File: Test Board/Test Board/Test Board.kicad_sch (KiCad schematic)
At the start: 51 parts, among them J10 Conn_Coaxial_Power, J11 Conn_Coaxial_Power, J13 Conn_Coaxial_Power, J8 Screw_Terminal_01x03, J9 Conn_Coaxial_Power, SW10 SW_SPDT, SW7 SW_SPDT, SW8 SW_SPDT, SW9 SW_SPDT, U27 OPA189, U28 BUF634A, U29 OPA189, U30 OPA189, U34 INA849

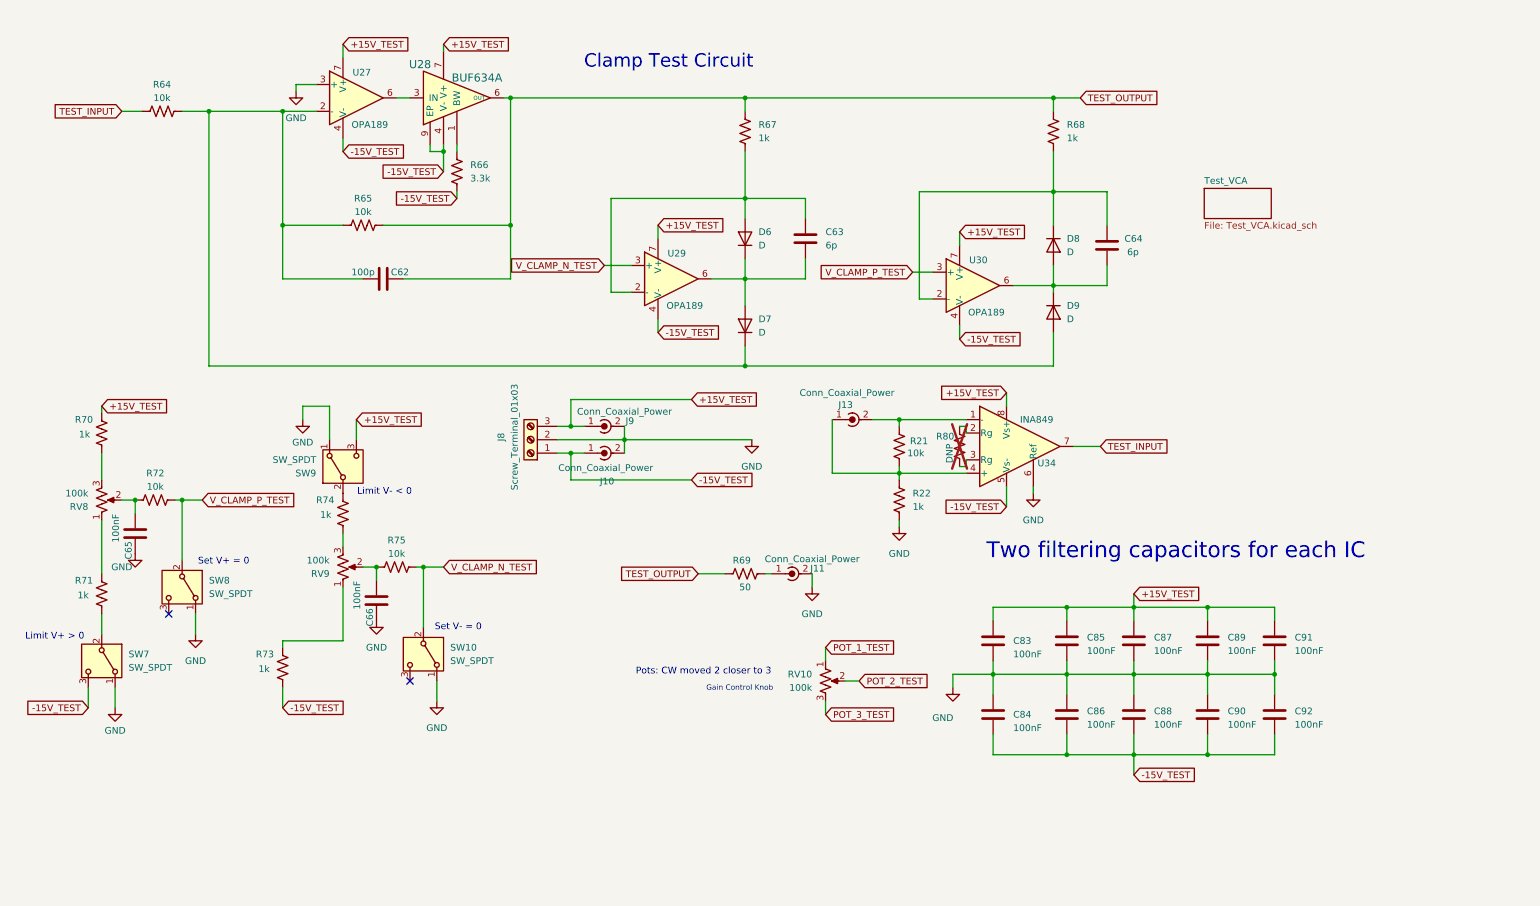
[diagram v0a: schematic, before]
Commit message: Removed LH circuit, added anti-windup test circuit, simplified voltage control mechanism
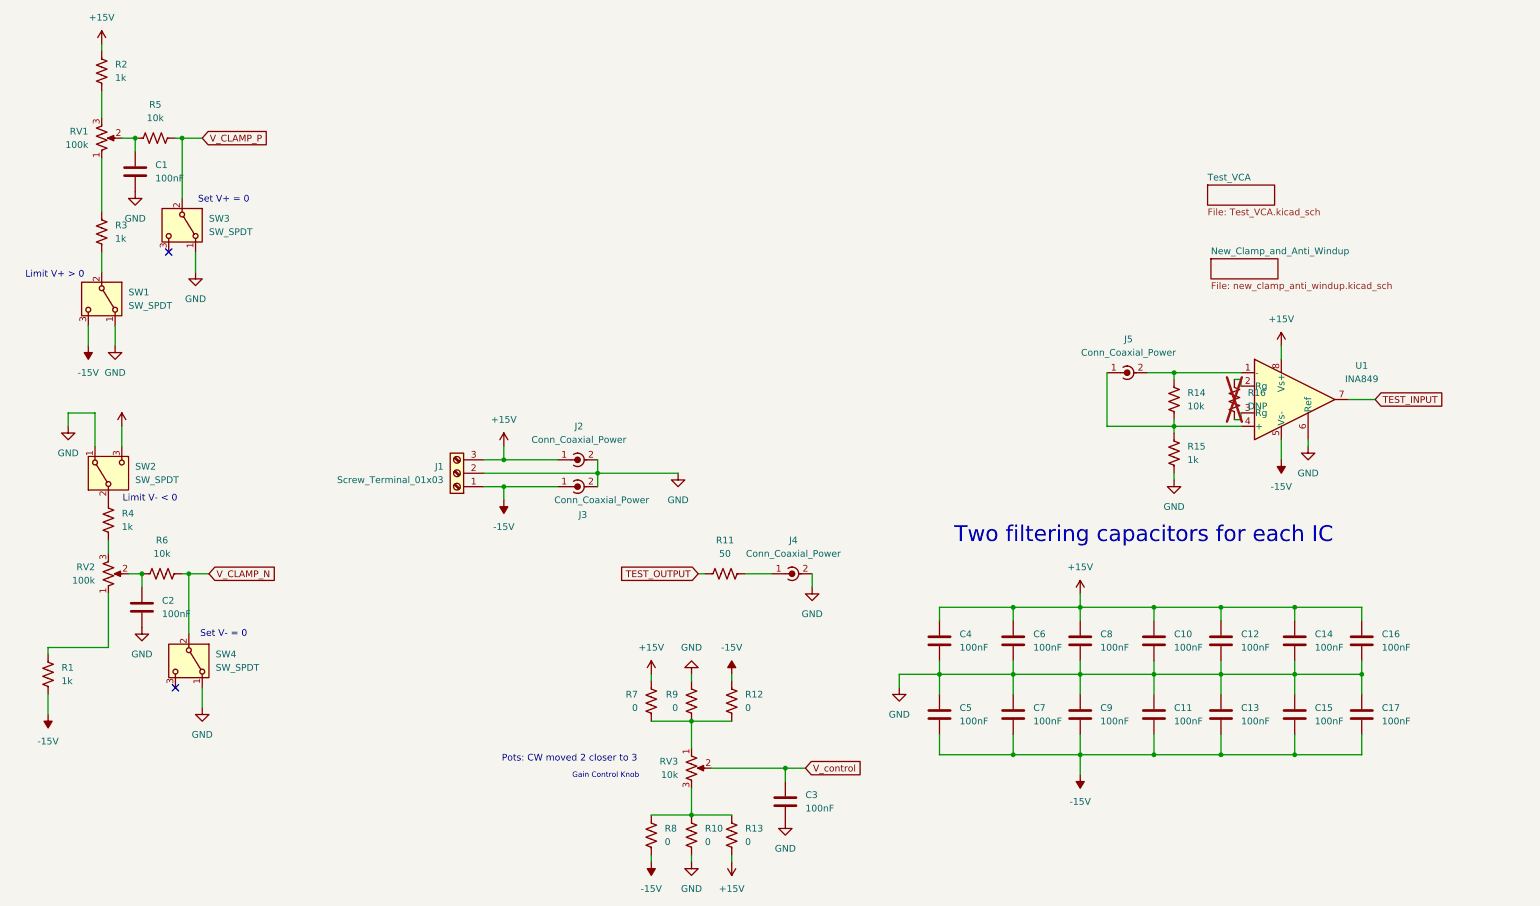
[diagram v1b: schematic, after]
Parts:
- removed C62: 100p, Capacitor_SMD:C_0805_2012Metric, symbol Device:C
- removed C63, C64: 6p, Capacitor_SMD:C_0805_2012Metric, symbol Device:C
- removed D6, D7, D8, D9: D, Package_TO_SOT_SMD:TSOT-23, symbol Device:D
- removed R64, R65: 10k, Resistor_SMD:R_0805_2012Metric, symbol Device:R_US
- removed R66: 3.3k, Resistor_SMD:R_0805_2012Metric, symbol Device:R_US
- removed R67, R68: 1k, Resistor_SMD:R_0805_2012Metric, symbol Device:R_US
- removed U27, U29, U30: OPA189, Package_SO:SOIC-8_3.9x4.9mm_P1.27mm, symbol Amplifier_Operational:OPA330xxD
- removed U28: BUF634A, Custom_Footprints:BUF634AIDDAR, symbol local_lib:BUF634A
- added C14, C15, C16, C17, C3: 100nF, Capacitor_SMD:C_0805_2012Metric, symbol Device:C
- added R10, R12, R13, R7, R8, R9: 0, Resistor_SMD:R_0805_2012Metric, symbol Device:R_US
- RV3: renamed from RV10; value 100k -> 10k
- renumbered C65 to C1, C89 to C10, C90 to C11, C91 to C12, C92 to C13, C66 to C2, C83 to C4, C84 to C5, C85 to C6, C86 to C7, C87 to C8, C88 to C9, J8 to J1, J9 to J2, J10 to J3, J11 to J4, J13 to J5, R73 to R1, R69 to R11, R21 to R14, R22 to R15, R80 to R16, R70 to R2, R71 to R3, R74 to R4, R72 to R5, R75 to R6, RV8 to RV1, RV9 to RV2, SW7 to SW1, SW9 to SW2, SW8 to SW3, SW10 to SW4, U34 to U1
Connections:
- net GND: now also C14.2, C15.1, C16.2, C17.1, C3.1, R10.2, R9.2
- net +15V_TEST renamed +15V
- net +15V: now also C14.1, C16.1, R13.2, R7.2
- net -15V_TEST renamed -15V
- net -15V: now also C15.2, C17.2, R12.2, R8.2
- net POT_1_TEST: no longer names the net of RV3.1
- net POT_1_TEST: now also R12.1, R7.1, R9.1
- net POT_2_TEST renamed V_control
- net V_control: now also C3.2
- net POT_3_TEST: no longer names the net of RV3.3
- net POT_3_TEST: now also R10.1, R13.1, R8.1
- net V_CLAMP_N_TEST renamed V_CLAMP_N
- net V_CLAMP_P_TEST renamed V_CLAMP_P
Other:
- added sheet New_Clamp_and_Anti_Windup (new_clamp_anti_windup.kicad_sch)
- note removed: "Clamp Test Circuit"
- moved on the sheet: C1, C10, C11, C12, C13, C2, C4, C5, C6, C7, C8, C9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

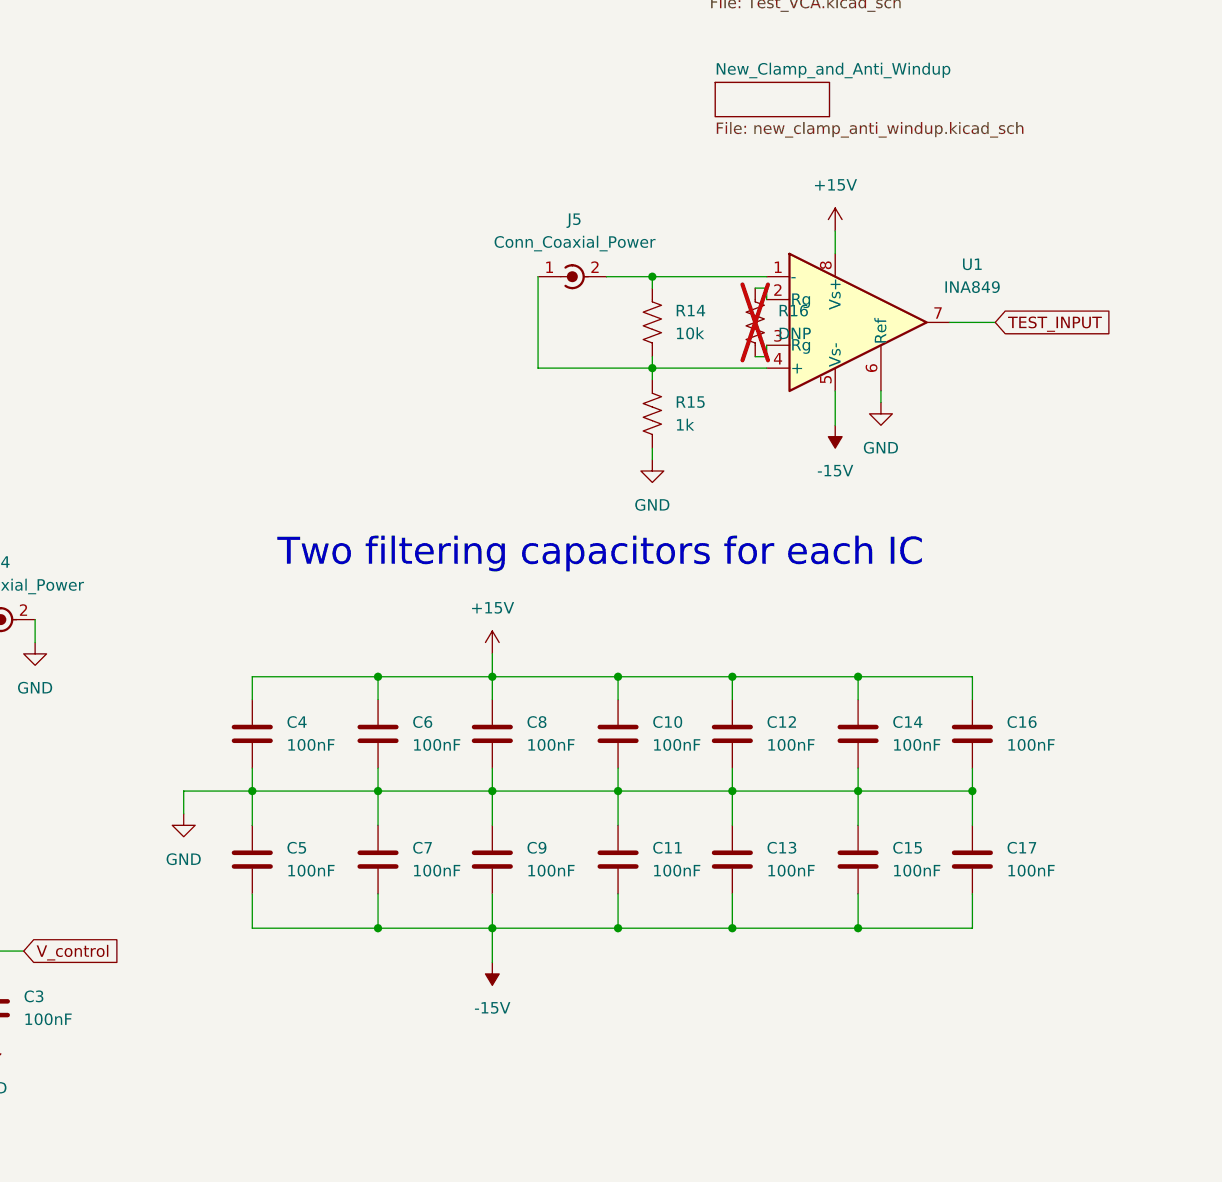
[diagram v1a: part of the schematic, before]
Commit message: First pass at routing Test Board, TODO: Find and Double check Part numbers
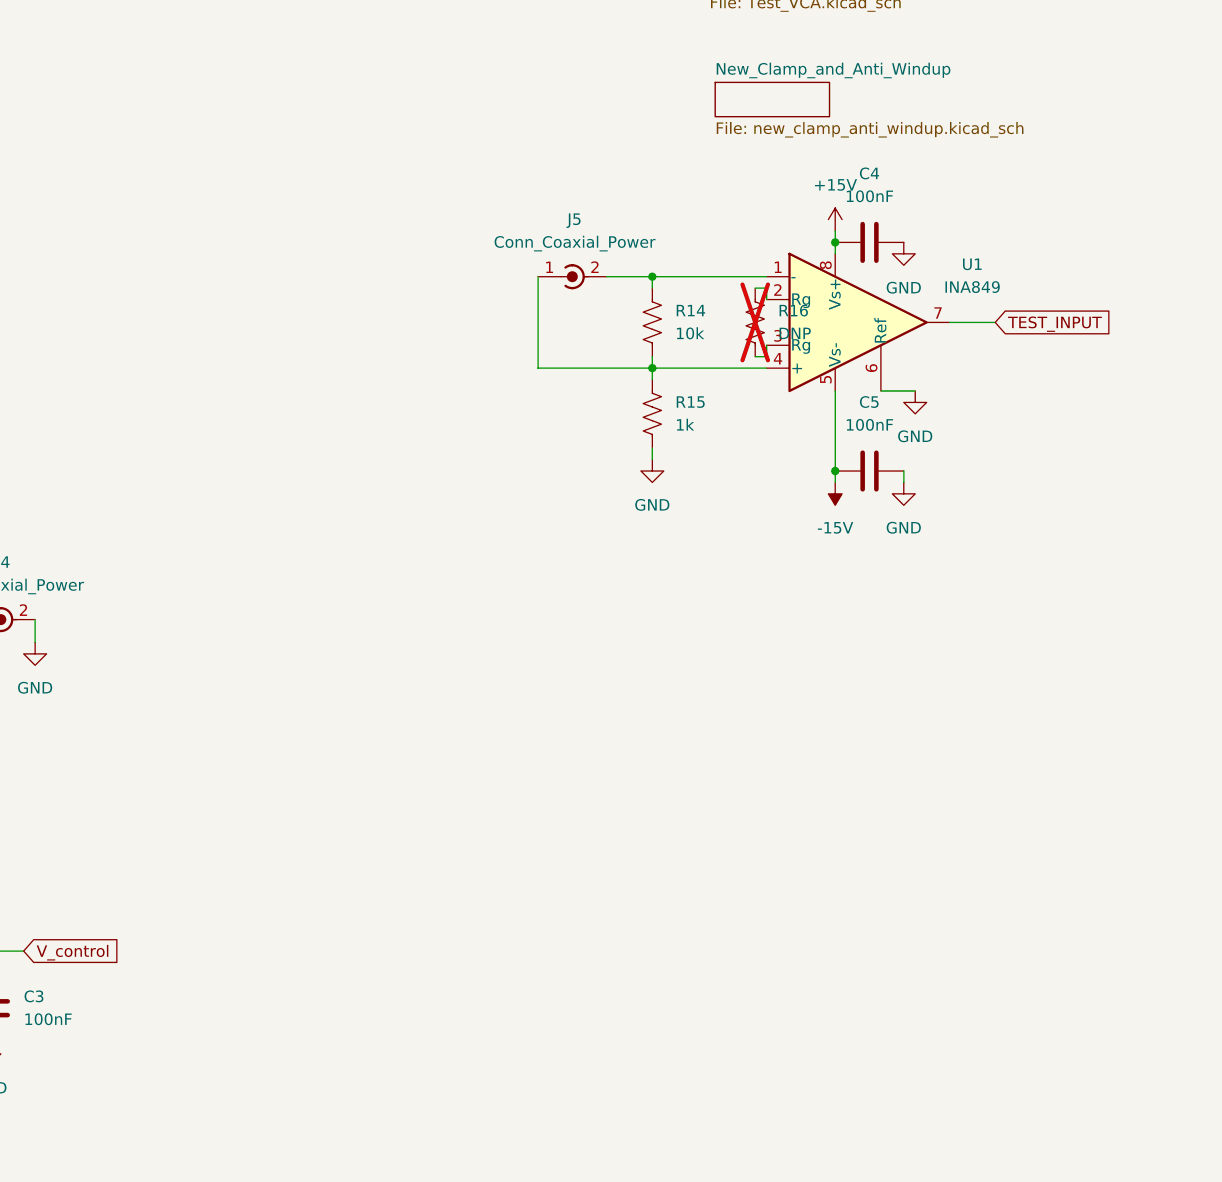
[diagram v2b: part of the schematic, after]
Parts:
- removed C10, C11, C12, C13, C14, C15, C16, C17, C6, C7, C8, C9: 100nF, Capacitor_SMD:C_0805_2012Metric, symbol Device:C
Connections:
- net -15V: now also C5.1; no longer C5.2
- net GND: now also C5.2; no longer C5.1
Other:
- note removed: "Two filtering capacitors for each IC"
- moved on the sheet: C4, C5
